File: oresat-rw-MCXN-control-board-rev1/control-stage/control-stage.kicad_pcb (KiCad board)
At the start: 6 copper layers, 40 x 36.5 mm, 99 parts, among them J1 Power Mezz, J2 Analog Mezz, J3 Phase Mezz, J4 ADCS Mezz, J5 Debug, J6 USB-C, J7 PROBE, Q1 TPN4R712MD,L1Q, SW1 BOOT0, SW2 RESET, U1 MCXN947VKLT, U2 TCAN330, U3 ADP7156ACPZ, U4 TLV62569DRL, Y1 24 MHz

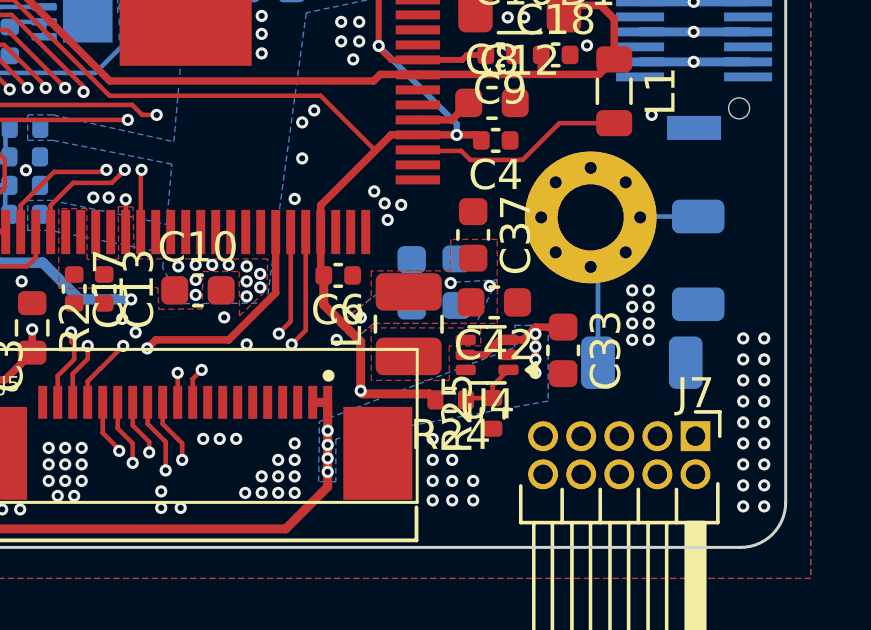
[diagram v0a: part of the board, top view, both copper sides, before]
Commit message: Small fixes on pre-fabbed board
Fixed Sch to PCB sync, updated footprints to library, OK'd DRCs, messed with 3.3VD SPS.
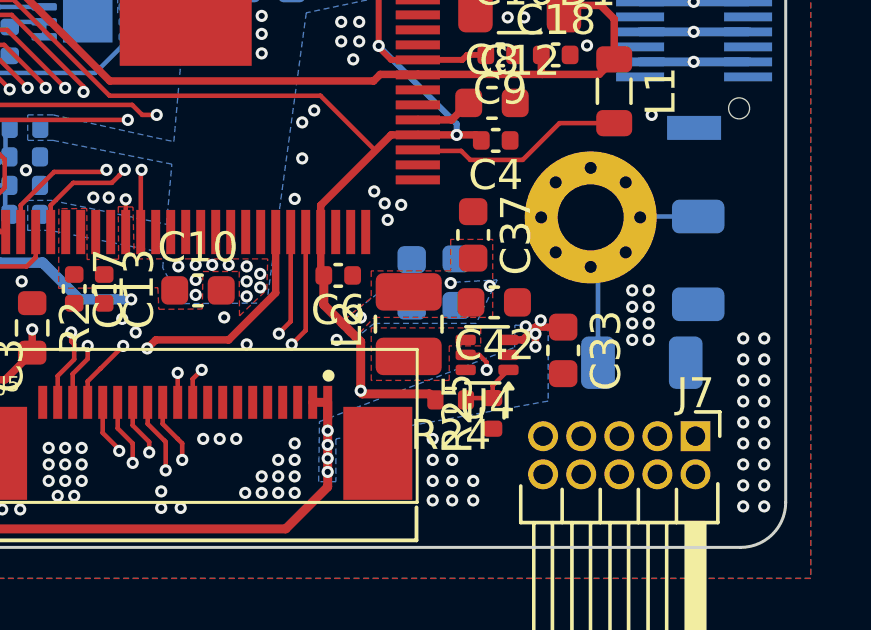
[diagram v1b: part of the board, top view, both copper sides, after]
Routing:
- net +5V: track 40.3 -> 38.8 mm, vias 27 -> 28

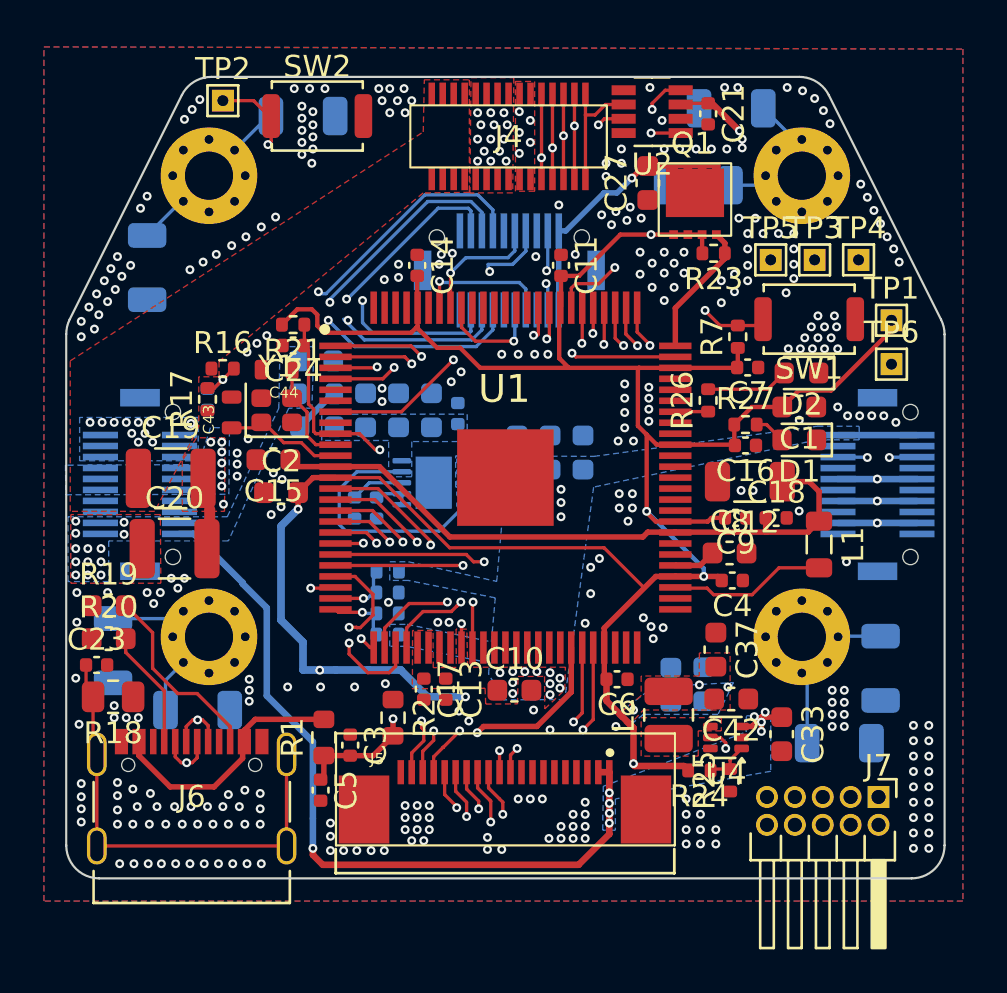
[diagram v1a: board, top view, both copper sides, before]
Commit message: Fixed 5V routing around 3.3v SMPS, added board silkscreen
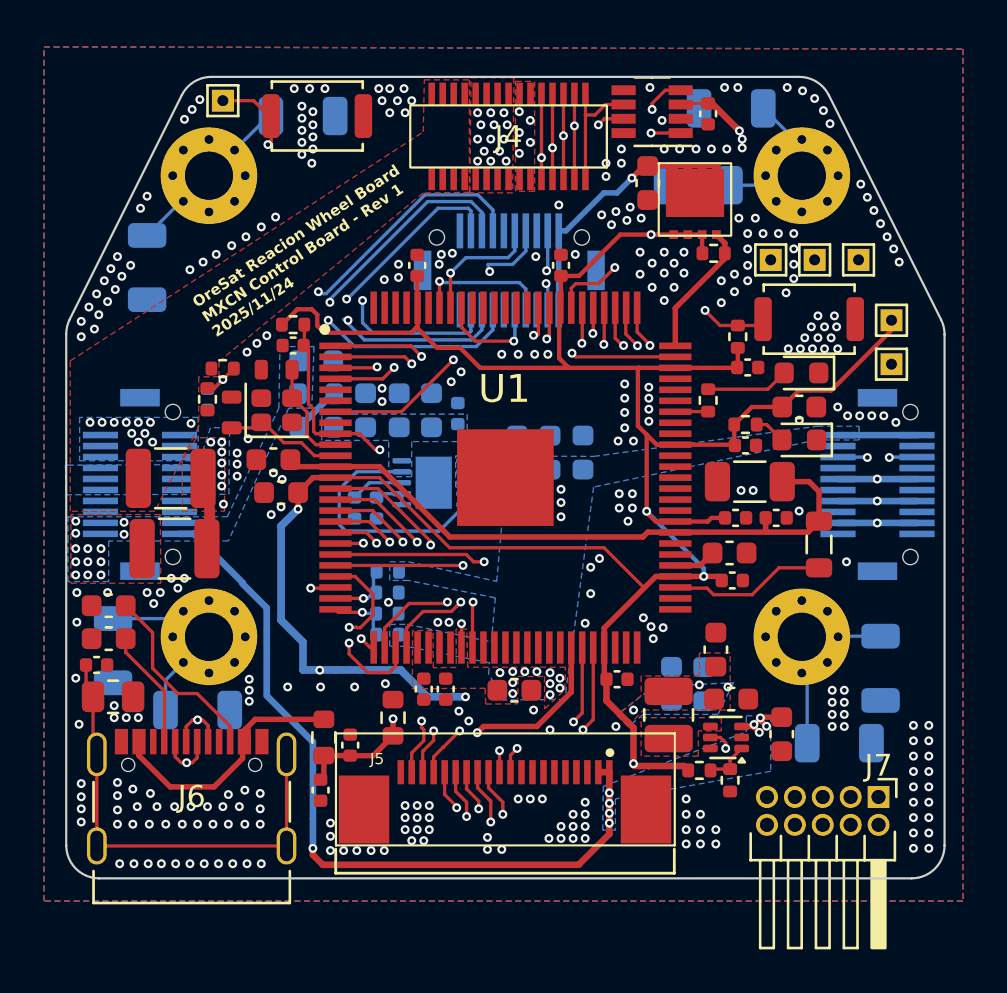
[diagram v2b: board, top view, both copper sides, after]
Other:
- board text added: "OreSat Reacion Wheel Board MXCN Control Board - Rev 1 2025/11/24"
